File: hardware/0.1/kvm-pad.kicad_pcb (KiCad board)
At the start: 2 copper layers, 76.2 x 64.1 mm, 96 parts, among them J1 USB_C_Receptacle_USB2.0, J2 USB_C_Receptacle_USB2.0, J3 AVR-ISP-6, J4 USB_A, J5 USB_A, J6 USB_A, K1 KEYSW, K2 KEYSW, K3 KEYSW, K4 KEYSW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

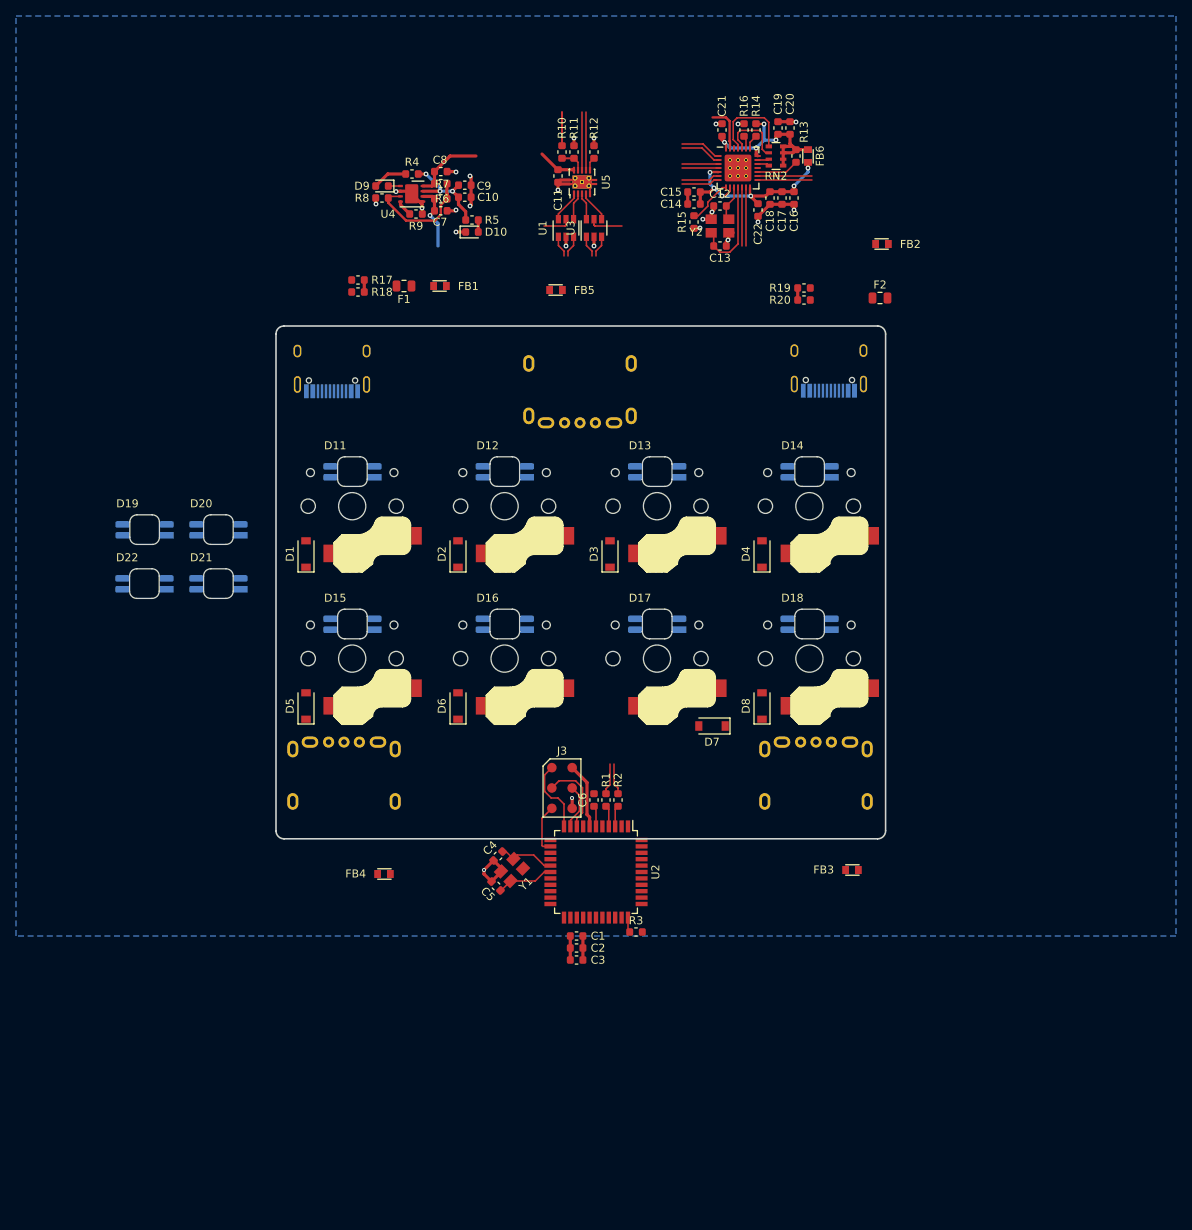
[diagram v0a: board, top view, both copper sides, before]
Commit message: alt layout
following what usb says... ;p
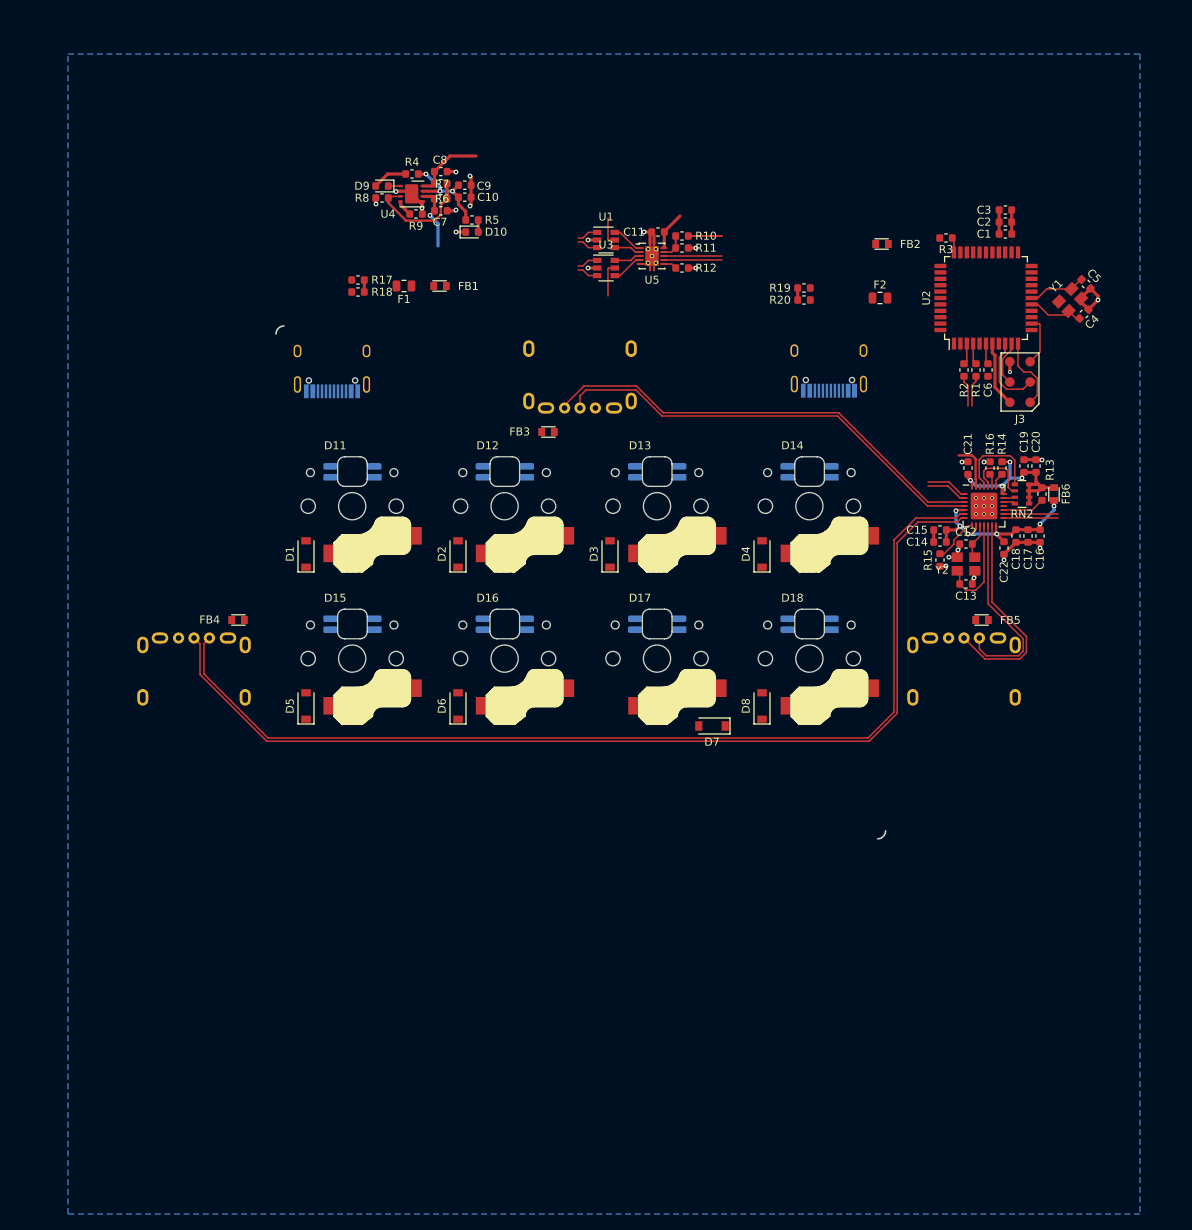
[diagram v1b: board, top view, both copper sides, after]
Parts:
- removed D19, D20, D21, D22: WS2812B, josh-led:SK8612-MINI-E
- moved C3 108.0 mm to (91.2, -14.5), turned to 180 degrees
- moved C2 105.4 mm to (91.2, -13.0), turned to 180 degrees
- moved C5 105.4 mm to (101.2, -5.25), turned to 315 degrees
- moved C1 102.8 mm to (91.2, -11.5), turned to 180 degrees
- moved C4 99.8 mm to (101.0, -1.50), turned to 45 degrees
- moved Y1 99.7 mm to (99.2, -3.25), turned to 45 degrees
- moved R3 95.0 mm to (83.8, -11.0), turned to 180 degrees
- moved U2 86.7 mm to (88.8, -3.50), turned to 90 degrees
- moved J3 76.5 mm to (93.0, 7.00), turned to 90 degrees
- moved C6 72.9 mm to (89.0, 5.50), turned to 270 degrees
- moved R1 70.9 mm to (87.5, 5.50), turned to 270 degrees
- moved R2 69.0 mm to (86.0, 5.50), turned to 270 degrees
- moved J4 68.4 mm to (38.0, 0.25), turned to 0 degrees
- moved FB5 67.4 mm to (88.2, 36.8)
- moved J6 67.1 mm to (86.0, 49.0), turned to 180 degrees
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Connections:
- D11 pad 4: Net-(D11-Pad4) -> /LED_DAT
- D15 pad 4: /LED_DAT -> Net-(D14-Pad2)
- U2 pad 20: /col1 -> Net-(U2-Pad20)
- U2 pad 21: /col2 -> Net-(U2-Pad21)
- U2 pad 22: /col4 -> Net-(U2-Pad22)
- U2 pad 25: /col3 -> Net-(U2-Pad25)
- U2 pad 40: /row2 -> Net-(U2-Pad40)
- U2 pad 41: /row1 -> Net-(U2-Pad41)
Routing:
- net /usb/D2_D+: track 5.10 -> 128.3 mm
- net /usb/D2_D-: track 4.76 -> 127.3 mm
- net /usb/D1_D-: track 4.55 -> 57.3 mm
- net /usb/D1_D+: track 4.55 -> 55.9 mm
- net /usb/D3_D+: track 7.30 -> 26.9 mm
- net /usb/D3_D-: track 7.30 -> 24.9 mm
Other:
- outline, holes or cut-outs redrawn
